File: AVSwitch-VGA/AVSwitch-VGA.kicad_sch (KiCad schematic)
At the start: 9 parts, among them J1 Conn_01x35_Pin, J2 DE15_Receptacle_HighDensity_M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, U1 SN74CBT3244PW

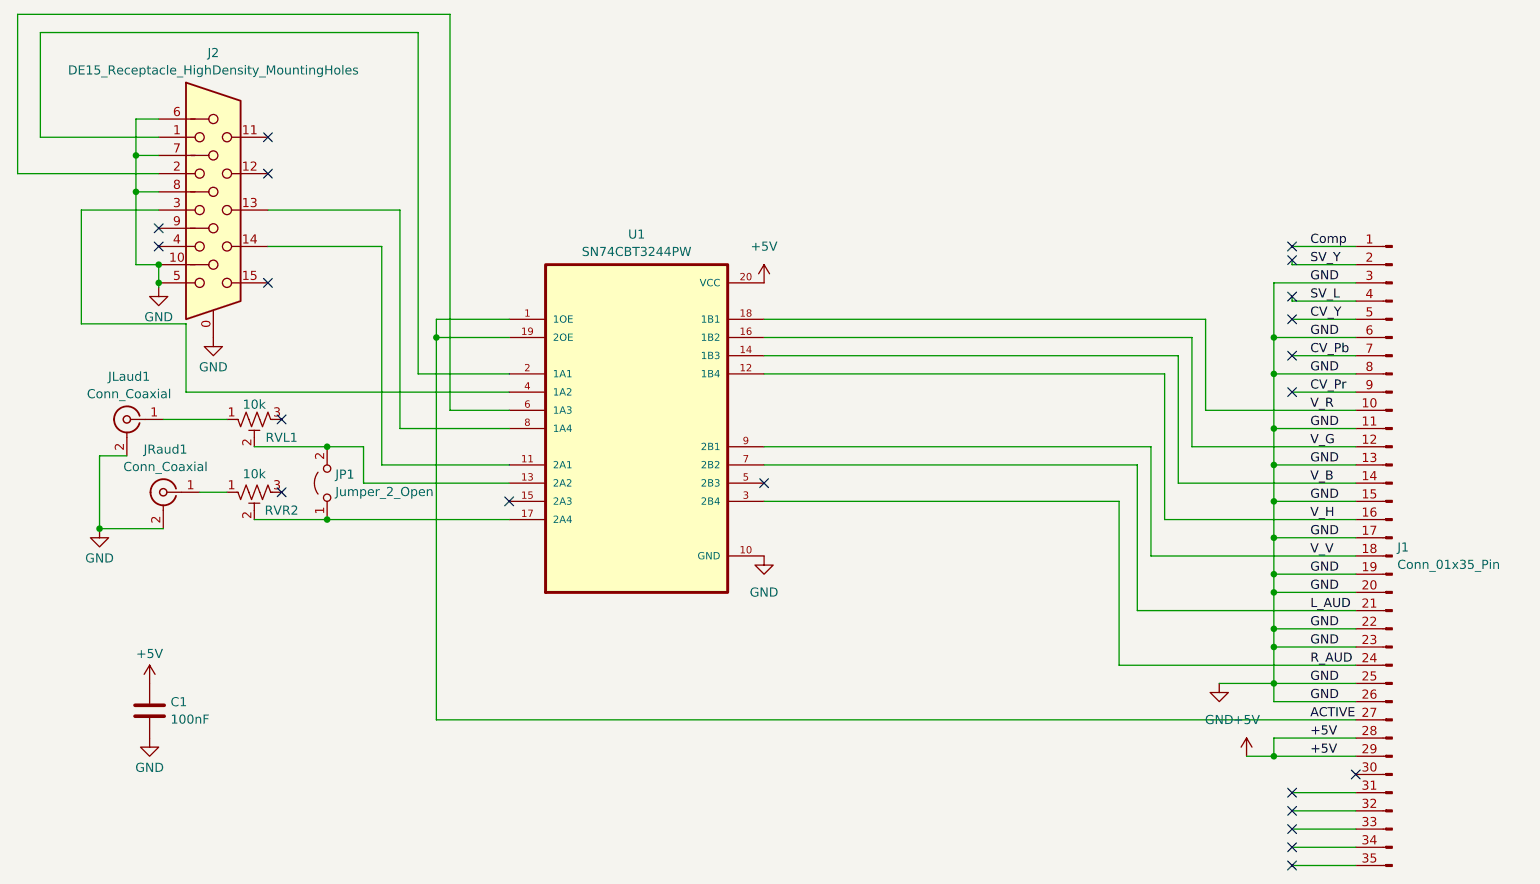
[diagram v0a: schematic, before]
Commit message: Add files via upload
New version with better footprint and ground isolation.
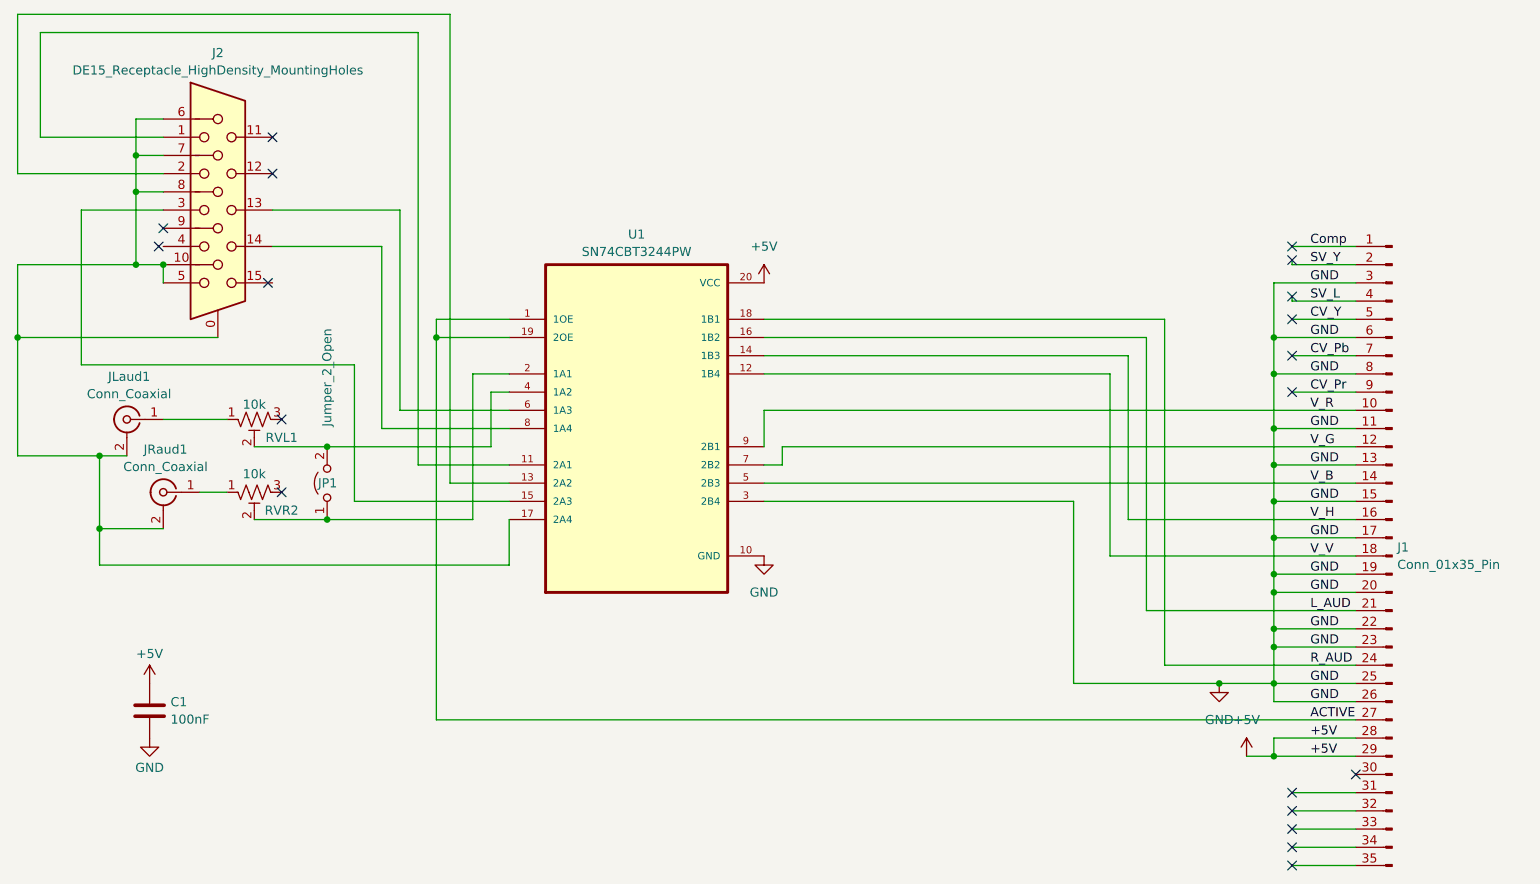
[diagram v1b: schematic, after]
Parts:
- U1: footprint Package_SO:TSSOP-20_4.4x6.5mm_P0.65mm -> Package_SO:SOIC-20W_7.5x12.8mm_P1.27mm
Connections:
- net GND: now also U1.3 (2B4); no longer J2.0, J2.10, J2.5, J2.6, J2.7, J2.8, JLaud1.2 (Ext), JRaud1.2 (Ext)
- net L_AUD: now also U1.16 (1B2); no longer U1.7 (2B2)
- net R_AUD: now also U1.18 (1B1); no longer U1.3 (2B4)
- net V_B: now also U1.5 (2B3); no longer U1.14 (1B3)
- net V_G: now also U1.7 (2B2); no longer U1.16 (1B2)
- net V_H: now also U1.14 (1B3); no longer U1.12 (1B4)
- net V_R: now also U1.9 (2B1); no longer U1.18 (1B1)
- net V_V: now also U1.12 (1B4); no longer U1.9 (2B1)
- net at JP1.1 (A), RVR2.2: now also U1.2 (1A1); no longer U1.17 (2A4)
- net at JP1.2 (B), RVL1.2: now also U1.4 (1A2); no longer U1.13 (2A2)
- net at U1.11 (2A1): now also J2.1; no longer J2.14
- net at U1.15 (2A3): now also J2.3
- net at J2.2: now also U1.13 (2A2); no longer U1.6 (1A3)
- net at J2.13: now also U1.6 (1A3); no longer U1.8 (1A4)
- new net: J2.0, J2.10, J2.5, J2.6, J2.7, J2.8, JLaud1.2 (Ext), JRaud1.2 (Ext), U1.17 (2A4)
- new net: J2.14, U1.8 (1A4)
- no-connect marks 21 -> 19
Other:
- moved on the sheet: J2
